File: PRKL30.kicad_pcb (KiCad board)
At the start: 2 copper layers, 254.9 x 62.2 mm, 103 parts, among them K1 KEYSW, K10 KEYSW, K11 KEYSW, K12 KEYSW, K14 KEYSW, K15 KEYSW, K16 KEYSW, K17 KEYSW, K18 KEYSW, K19 KEYSW, K2 KEYSW, K20 KEYSW, K21 KEYSW, K22 KEYSW, K23 KEYSW, K24 KEYSW, K25 KEYSW, K27 KEYSW, K28 KEYSW, K29 KEYSW, K3 KEYSW, K30 KEYSW, K31 KEYSW, K32 KEYSW, K33 KEYSW, K34 KEYSW, K35 KEYSW, K36 KEYSW, K37 KEYSW, K4 KEYSW, K5 KEYSW, K6 KEYSW, K7 KEYSW, K8 KEYSW, K9 KEYSW, M3_1 VAL**, M3_2 VAL**, M3_3 VAL**, M3_4 VAL**, M3_5 VAL**, M3_6 VAL**, M3_7 VAL**, SW2 SW_SPDT

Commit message: Add files via upload
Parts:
- removed the G*** at (282.4, 91.2)
- removed the G*** at (303.0, 99.8) (x2)
- removed the G*** at (67.6, 95.0)
- removed the G*** at (282.7, 90.9)
- removed the G*** at (145.5, 94.7)
- removed the G*** at (181.1, 92.7)
- removed the G*** at (294.4, 65.0)
- removed the G*** at (220.0, 98.3)
- added G***: LOGO, MEEMIKEEBSILK:PRKL30SILK, B.Cu at (255.8, 87.9)
- added G***: LOGO, MEEMIKEEBSILK:Logo, B.Cu at (280.4, 91.9)
- moved G*** 107.0 mm to (214.4, 84.1)

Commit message: Prototype version
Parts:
- ?: renamed from G***; value LOGO -> (none)
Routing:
- net Net-(D6-Pad2): track 16.6 -> 13.5 mm
- net Net-(D15-Pad2): track 15.7 -> 12.8 mm
- net Net-(D5-Pad2): track 15.7 -> 13.0 mm
- net Net-(D2-Pad2): track 15.5 -> 13.2 mm
- net Net-(D7-Pad2): track 16.8 -> 14.5 mm
- net Net-(D12-Pad2): track 17.1 -> 14.8 mm
- net Net-(D9-Pad2): track 16.8 -> 14.5 mm
- net Net-(D8-Pad2): track 17.1 -> 14.8 mm
- net Net-(D11-Pad2): track 16.8 -> 14.5 mm
- net Net-(D1-Pad2): track 21.3 -> 19.3 mm
- net Net-(D10-Pad2): track 17.2 -> 15.7 mm
- net Net-(D28-Pad2): track 15.2 -> 13.7 mm
- net Net-(D13-Pad2): track 19.4 -> 17.9 mm
- net Net-(D3-Pad2): track 27.6 -> 26.3 mm
- net Net-(D4-Pad2): track 19.9 -> 18.7 mm
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
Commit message: Rotate one diode footprint, Add silkscreen text for underglow pins, fix autoroute mistakes
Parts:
- LED_DATA1: value 0 -> LED_DATA
- LED_GND1: value 0 -> LED_GND
- LED_PWR1: value 0 -> LED_PWR
- moved D18 17.9 mm to (129.9, 83.8)
- moved D17 1.36 mm to (127.3, 83.8)
- turned D37 to 90 degrees
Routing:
- net RowB: track 241.8 -> 230.7 mm, vias 1 -> 3
- net RowD: track 275.4 -> 284.9 mm
- net Net-(D18-Pad2): track 21.3 -> 15.7 mm
- net Net-(D37-Pad2): track 21.9 -> 19.5 mm
- net Net-(D17-Pad2): track 19.6 -> 17.4 mm
- net Net-(D31-Pad2): track 19.5 -> 17.5 mm
- net Net-(D33-Pad2): track 22.4 -> 20.4 mm
- net Net-(D30-Pad2): track 23.4 -> 21.4 mm
- net ColF: track 330.5 -> 328.5 mm
- net Net-(D35-Pad2): track 20.1 -> 18.9 mm
- net Net-(D34-Pad2): track 20.0 -> 18.7 mm
- net Net-(D32-Pad2): track 28.9 -> 27.7 mm
- net Net-(D29-Pad2): track 38.9 -> 37.7 mm
- net Net-(D27-Pad2): track 19.3 -> 18.1 mm
- net Net-(D36-Pad2): track 19.8 -> 18.6 mm
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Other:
- board text removed: "WS2812"

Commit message: mc's flipped, pro micro moved, silks fixed, reset button and diodes moved
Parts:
- removed the G*** at (280.4, 91.9)
- removed the G*** at (214.4, 84.1)
- added G***: LOGO, MEEMIKEEBSILK:Pb, B.Cu at (100.1, 94.0)
- MCU_Pro_Micr0: moved to F.Cu
- moved SW_RST1 114.3 mm to (261.9, 76.2), turned to 0 degrees
- moved D3 46.0 mm to (127.5, 66.5), turned to 90 degrees
- moved Feather1 25.3 mm to (99.6, 102.9), turned to 90 degrees
- moved D23 19.3 mm to (224.0, 84.0)
- moved D22 19.1 mm to (205.0, 83.8)
- moved D21 18.9 mm to (185.9, 83.7)
- moved D20 18.7 mm to (167.1, 83.6)
- moved D24 18.1 mm to (242.8, 84.3)
- moved D19 17.4 mm to (149.4, 83.3)
- moved D18 17.0 mm to (146.8, 83.3)
- moved D5 16.5 mm to (146.6, 66.8)
- moved D16 11.9 mm to (127.5, 83.8), turned to 90 degrees
- moved D33 3.63 mm to (185.7, 104.7)
- moved D35 3.46 mm to (224.3, 104.6)
- moved MCU_Pro_Micr0 3.00 mm to (100.0, 70.4)
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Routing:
- net ColF: track 328.5 -> 0.00 mm
- net GND: track 299.2 -> 0.00 mm, vias 1 -> 0
- net ColC: track 287.9 -> 0.00 mm
- net RowD: track 284.9 -> 0.00 mm
- net ColB: track 273.0 -> 0.00 mm
- net ColH: track 268.6 -> 0.00 mm, vias 1 -> 0
- net ColA: track 267.3 -> 0.00 mm
- net ColD: track 255.2 -> 0.00 mm
- net ColE: track 253.9 -> 0.00 mm, vias 2 -> 0
- net RowC: track 244.5 -> 0.00 mm
- net ColG: track 238.5 -> 0.00 mm
- net RowB: track 230.7 -> 0.00 mm, vias 3 -> 0
- net RowA: track 215.9 -> 0.00 mm
- net ColJ: track 212.2 -> 0.00 mm
- net DP1: track 209.4 -> 0.00 mm
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
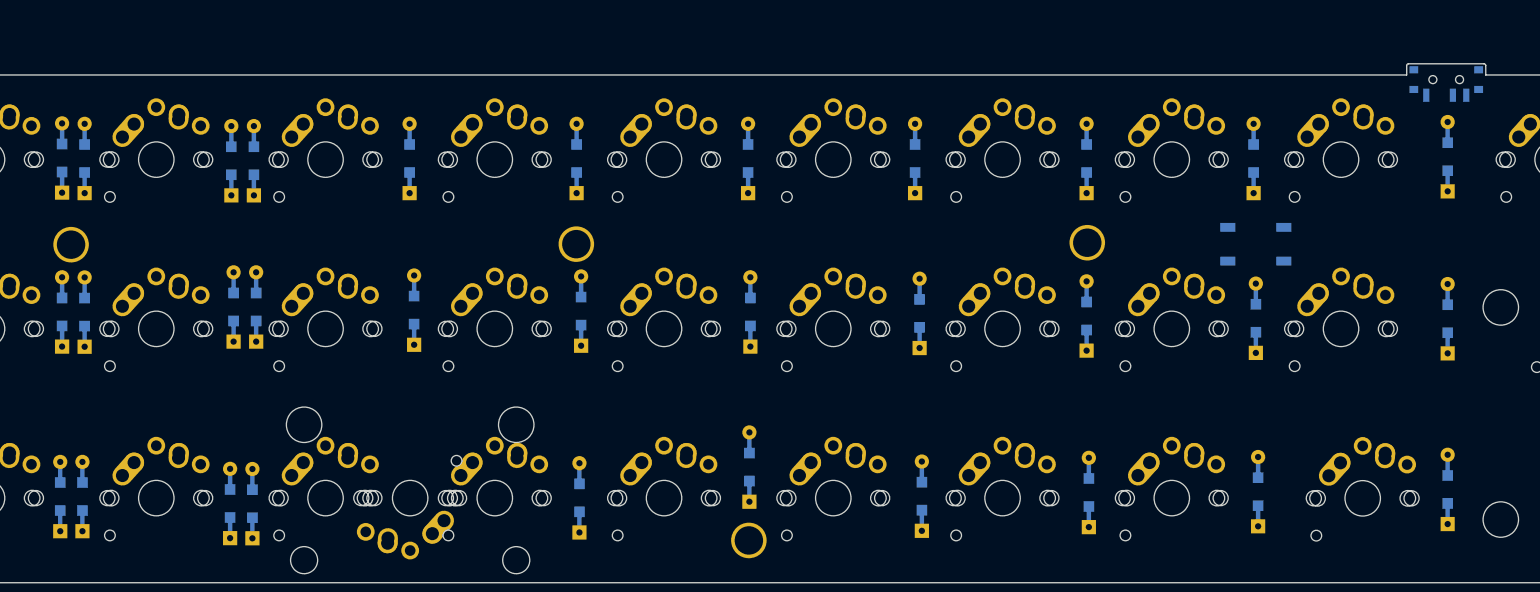
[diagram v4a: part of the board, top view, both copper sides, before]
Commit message: Move bluetooth switch, make room for battery between middle standoffs
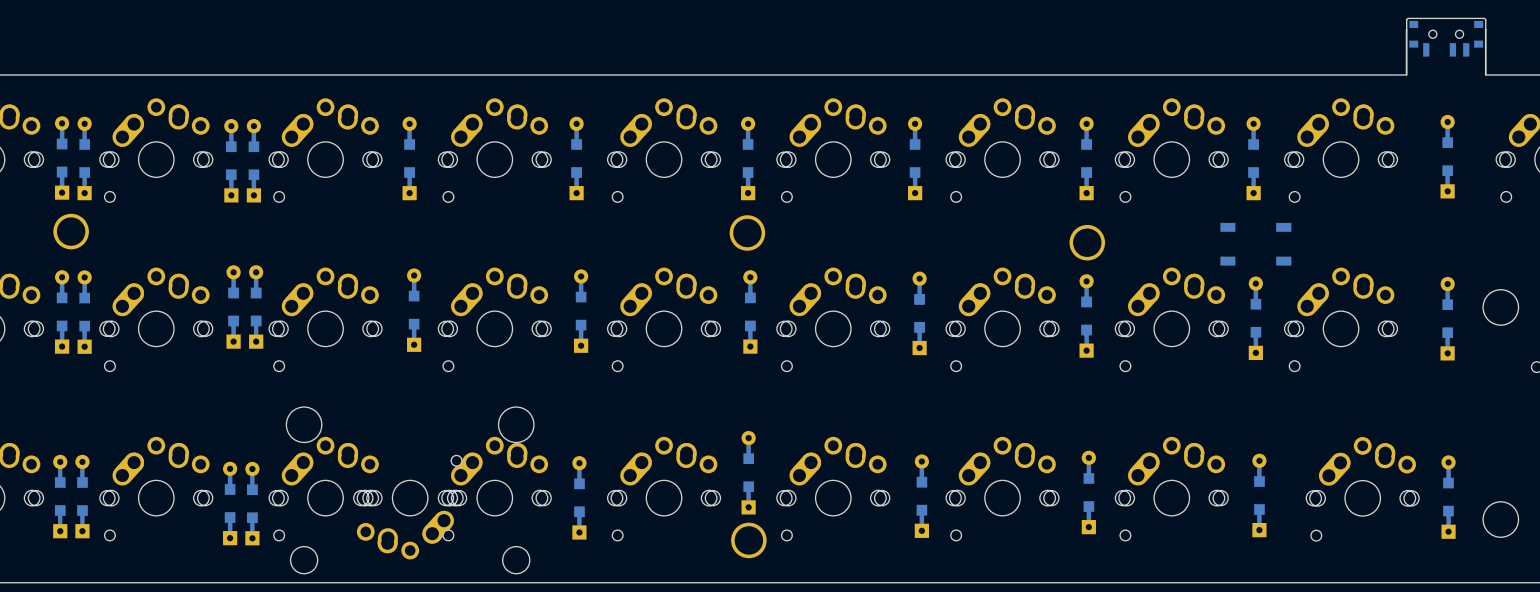
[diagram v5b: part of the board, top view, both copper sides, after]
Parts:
- moved M3_4 19.3 mm to (204.6, 74.9)
- moved SW2 5.11 mm to (283.3, 52.9)
- moved M3_3 1.47 mm to (128.5, 74.8)
- moved D_1.25u1 0.87 mm to (283.6, 104.7)
- moved D34 0.64 mm to (204.8, 101.9)
- moved D37 0.45 mm to (262.3, 104.5)
- renumbered G*** to G_PB, G*** to G_silk_gfx
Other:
- board size 254.9 x 62.2 mm -> 254.9 x 63.5 mm
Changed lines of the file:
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@@
-(kicad_pcb (version 20171130) (host pcbnew "(5.1.5)-3")
+(kicad_pcb (version 20171130) (host pcbnew "(5.0.1)-3")
   (general
     (thickness 1.6)
-    (drawings 22)
+    (drawings 24)
     (tracks 0)
     (zones 0)
@@
     (zone_45_only no)
     (trace_min 0.2)
+    (segment_width 0.2)
+    (edge_width 0.15)
     (via_size 0.8)
     (via_drill 0.4)
@@
     (uvia_min_size 0.2)
     (uvia_min_drill 0.1)
-    (edge_width 0.15)
-    (segment_width 0.2)
     (pcb_text_width 0.3)
     (pcb_text_size 1.5 1.5)
@@
     (mod_text_size 1 1)
     (mod_text_width 0.15)
-    (pad_size 1.524 1.524)
-    (pad_drill 0.762)
+    (pad_size 3.2 2)
+    (pad_drill 2.8)
     (pad_to_mask_clearance 0.051)
     (solder_mask_min_width 0.25)
@@
     (at 146.558 66.802 90)
     (attr smd)
-    (fp_text reference D5 (at 0 -1.925 90) (layer B.SilkS)
+    (fp_text reference D5 (at 0 0 90) (layer B.SilkS)
       (effects (font (size 0.8 0.8) (thickness 0.15)) (justify mirror))
     )
@@
   (module MEEMIKEEBSILK:Pb (layer B.Cu)
     (at 100.076 93.98 180)
-    (fp_text reference G*** (at 0 0 180) (layer F.SilkS) hide
+    (fp_text reference G_PB (at 0 0 180) (layer F.SilkS) hide
       (effects (font (size 1.524 1.524) (thickness 0.3)))
     )
@@
   (module MEEMIKEEBSILK:PRKL30SILK (layer B.Cu)
     (at 255.778 87.884 180)
-    (fp_text reference G*** (at 76.2 13.97 180) (layer F.SilkS) hide
+    (fp_text reference G_silk_gfx (at 76.2 13.97 180) (layer F.SilkS) hide
       (effects (font (size 1.524 1.524) (thickness 0.3)))
     )
@@
     (at 130.048 66.548 90)
     (attr smd)
-    (fp_text reference D4 (at 0 -1.925 90) (layer B.SilkS)
+    (fp_text reference D4 (at 0 0 90) (layer B.SilkS)
       (effects (font (size 0.8 0.8) (thickness 0.15)) (justify mirror))
     )
@@
     (at 70.3 67.056 90)
     (attr smd)
-    (fp_text reference D1 (at 0 -1.925 90) (layer B.SilkS)
+    (fp_text reference D1 (at 0 0 90) (layer B.SilkS)
       (effects (font (size 0.8 0.8) (thickness 0.15)) (justify mirror))
     )
@@
     (at 72.644 67.056 90)
     (attr smd)
-    (fp_text reference D2 (at 0 -1.925 90) (layer B.SilkS)
+    (fp_text reference D2 (at 0 0 90) (layer B.SilkS)
       (effects (font (size 0.8 0.8) (thickness 0.15)) (justify mirror))
     )
@@
     (at 127.508 66.497 90)
     (attr smd)
-    (fp_text reference D3 (at 0 -1.925 90) (layer B.SilkS)
+    (fp_text reference D3 (at 0 0 90) (layer B.SilkS)
       (effects (font (size 0.8 0.8) (thickness 0.15)) (justify mirror))
     )
@@
     (at 149.098 66.802 90)
     (attr smd)
-    (fp_text reference D6 (at 0 -1.925 90) (layer B.SilkS)
+    (fp_text reference D6 (at 0 0 90) (layer B.SilkS)
       (effects (font (size 0.8 0.8) (thickness 0.15)) (justify mirror))
     )
@@
     (at 127.508 83.82 90)
     (attr smd)
-    (fp_text reference D16 (at 0 -1.925 90) (layer B.SilkS)
+    (fp_text reference D16 (at 0 0 90) (layer B.SilkS)
       (effects (font (size 0.8 0.8) (thickness 0.15)) (justify mirror))
     )
@@
     (at 130.048 83.836 90)
     (attr smd)
-    (fp_text reference D17 (at 0 -1.925 90) (layer B.SilkS)
+    (fp_text reference D17 (at 0 0 90) (layer B.SilkS)
       (effects (font (size 0.8 0.8) (thickness 0.15)) (justify mirror))
     )
@@
     (at 146.812 83.261 90)
     (attr smd)
-    (fp_text reference D18 (at 0 -1.925 90) (layer B.SilkS)
+    (fp_text reference D18 (at 0 0 90) (layer B.SilkS)
       (effects (font (size 0.8 0.8) (thickness 0.15)) (justify mirror))
     )
@@
     (at 149.352 83.261 90)
     (attr smd)
-    (fp_text reference D19 (at 0 -1.925 90) (layer B.SilkS)
+    (fp_text reference D19 (at 0 0 90) (layer B.SilkS)
       (effects (font (size 0.8 0.8) (thickness 0.15)) (justify mirror))
     )
@@
     (at 70.3 104.4 90)
     (attr smd)
-    (fp_text reference D27 (at 0.006 -1.212 90) (layer B.SilkS)
+    (fp_text reference D27 (at 0.006 0 90) (layer B.SilkS)
       (effects (font (size 0.8 0.8) (thickness 0.15)) (justify mirror))
     )
@@
     (at 72.8 104.3 90)
     (attr smd)
-    (fp_text reference D28 (at -0.094 1.114 90) (layer B.SilkS)
+    (fp_text reference D28 (at -0.094 0 90) (layer B.SilkS)
       (effects (font (size 0.8 0.8) (thickness 0.15)) (justify mirror))
     )
@@
     (at 127.3 104.6 90)
     (attr smd)
-    (fp_text reference D29 (at 0 -1.925 90) (layer B.SilkS)
+    (fp_text reference D29 (at 0 0 90) (layer B.SilkS)
       (effects (font (size 0.8 0.8) (thickness 0.15)) (justify mirror))
     )
@@
     (at 129.8 104.6 90)
     (attr smd)
-    (fp_text reference D30 (at 0 -1.925 90) (layer B.SilkS)
+    (fp_text reference D30 (at 0 0 90) (layer B.SilkS)
       (effects (font (size 0.8 0.8) (thickness 0.15)) (justify mirror))
     )
@@
     (at 146.42 105.38 90)
     (attr smd)
-    (fp_text reference D31 (at 0 -1.925 90) (layer B.SilkS)
+    (fp_text reference D31 (at 0 0 90) (layer B.SilkS)
       (effects (font (size 0.8 0.8) (thickness 0.15)) (justify mirror))
     )
@@
     (at 148.93 105.4 90)
     (attr smd)
-    (fp_text reference D32 (at 0 -1.925 90) (layer B.SilkS)
+    (fp_text reference D32 (at 0 0 90) (layer B.SilkS)
       (effects (font (size 0.8 0.8) (thickness 0.15)) (justify mirror))
     )
@@
   )
   (module keyboard_parts:D_SOD123_axial (layer B.Cu)
-    (at 204.87 101.28 90)
+    (at 204.786 101.916 90)
     (attr smd)
     (fp_text reference D34 (at 0 -1.925 90) (layer B.SilkS)
@@
   )
   (module keyboard_parts:D_SOD123_axial (layer B.Cu)
-    (at 262.128 104.05 90)
+    (at 262.276 104.476 90)
     (attr smd)
     (fp_text reference D37 (at 0 -1.925 90) (layer B.SilkS)
@@
   )
   (module keyboard_parts:D_SOD123_axial (layer B.Cu)
-    (at 283.464 103.796 90)
+    (at 283.566 104.656 90)
     (attr smd)
     (fp_text reference D_1.25u1 (at 0 -1.925 270) (layer B.SilkS)
@@
   )
   (module Button_Switch_SMD:SW_SPDT_PCM12 (layer B.Cu)
-    (at 283.3 58)
+    (at 283.3 52.8946)
     (descr "Ultraminiature Surface Mount Slide Switch, right-angle, https://www.ckswitches.com/media/1424/pcm.pdf")
     (attr smd)
@@
   )
   (module keyboard_parts:HOLE_M3 (layer F.Cu)
-    (at 128.52 76.25)
+    (at 128.526 74.776)
     (fp_text reference M3_3 (at 0 -4.5) (layer F.SilkS) hide
       (effects (font (size 1.524 1.524) (thickness 0.3048)))
@@
   )
   (module keyboard_parts:HOLE_M3 (layer F.Cu)
-    (at 185.39 76.19)
+    (at 204.646 74.936)
     (fp_text reference M3_4 (at 0 -4.5) (layer F.SilkS) hide
       (effects (font (size 1.524 1.524) (thickness 0.3048)))
@@
     (pad 1 thru_hole circle (at 0 0) (size 4 4) (drill 3.2) (layers *.Cu *.Mask F.SilkS))
   )
+  (gr_line (start 278.846 52.036) (end 278.846 57.126) (layer Edge.Cuts) (width 0.2))
+  (gr_line (start 287.756 52.046) (end 287.756 57.126) (layer Edge.Cuts) (width 0.2))
   (gr_arc (start 87.74 56.15) (end 87.74 57.15) (angle -90) (layer Edge.Cuts) (width 0.15))
   (gr_arc (start 53.38 58.14) (end 53.38 57.14) (angle -90) (layer Edge.Cuts) (width 0.15))
-  (gr_line (start 279.05 55.89) (end 287.55 55.89) (layer Edge.Cuts) (width 0.15))
-  (gr_line (start 287.75 57.15) (end 287.75 56.09) (layer Edge.Cuts) (width 0.15))
-  (gr_line (start 278.85 57.15) (end 278.85025 56.099988) (layer Edge.Cuts) (width 0.15))
-  (gr_arc (start 279.05 56.09) (end 279.05 55.89) (angle -92.86240523) (layer Edge.Cuts) (width 0.15))
-  (gr_arc (start 287.55 56.09) (end 287.75 56.09) (angle -90) (layer Edge.Cuts) (width 0.15))
+  (gr_line (start 279.05 50.7846) (end 287.55 50.7846) (layer Edge.Cuts) (width 0.15))
+  (gr_line (start 287.75 52.0446) (end 287.75 50.9846) (layer Edge.Cuts) (width 0.15))
+  (gr_line (start 278.85 52.0446) (end 278.85025 50.994588) (layer Edge.Cuts) (width 0.15))
+  (gr_arc (start 279.05 50.9846) (end 279.05 50.7846) (angle -92.86240523) (layer Edge.Cuts) (width 0.15))
+  (gr_arc (start 287.55 50.9846) (end 287.75 50.9846) (angle -90) (layer Edge.Cuts) (width 0.15))
   (gr_line (start 306.23 114.3) (end 53.37 114.29995) (layer Edge.Cuts) (width 0.15))
   (gr_line (start 52.38 113.3) (end 52.38 58.14) (layer Edge.Cuts) (width 0.15))

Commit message: Add new routings, change mounting holes to M2
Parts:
- removed ?: , MEEMIKEEBSILK:PRKLplain
- Feather1: value Adafruit32u4BLE -> Adafruit_32u4BLE
- G_PB: value LOGO -> LOGO_PB
- G_silk_gfx: value LOGO -> LOGO_GFX
- K_2Uspc1: value KEYSW -> KEYSW_2u
- M2_1: renamed from M3_1; footprint keyboard_parts:HOLE_M3 -> MountingHole:MountingHole_2.2mm_M2
- M2_2: renamed from M3_2; footprint keyboard_parts:HOLE_M3 -> MountingHole:MountingHole_2.2mm_M2
- M2_3: renamed from M3_3; footprint keyboard_parts:HOLE_M3 -> MountingHole:MountingHole_2.2mm_M2
- M2_4: renamed from M3_4; footprint keyboard_parts:HOLE_M3 -> MountingHole:MountingHole_2.2mm_M2
- M2_5: renamed from M3_5; footprint keyboard_parts:HOLE_M3 -> MountingHole:MountingHole_2.2mm_M2
- M2_6: renamed from M3_6; footprint keyboard_parts:HOLE_M3 -> MountingHole:MountingHole_2.2mm_M2
- M2_7: renamed from M3_7; footprint keyboard_parts:HOLE_M3 -> MountingHole:MountingHole_2.2mm_M2
- MCU_Pro_Micr0: value ProMicro -> Pro_Micro
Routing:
- net RowD: track 0.00 -> 315.8 mm
- net GND: track 0.00 -> 308.7 mm, vias 0 -> 1
- net ColF: track 0.00 -> 289.9 mm
- net ColB: track 0.00 -> 286.3 mm
- net ColA: track 0.00 -> 263.7 mm
- net ColC: track 0.00 -> 256.6 mm
- net ColE: track 0.00 -> 243.9 mm
- net RowC: track 0.00 -> 240.5 mm
- net ColH: track 0.00 -> 230.4 mm, vias 0 -> 1
- net ColG: track 0.00 -> 224.6 mm
- net RowA: track 0.00 -> 206.9 mm
- net ColD: track 0.00 -> 206.1 mm
- net RowB: track 0.00 -> 199.0 mm
- net ColJ: track 0.00 -> 195.2 mm
- net RST: track 0.00 -> 185.3 mm
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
